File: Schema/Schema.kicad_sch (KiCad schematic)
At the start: 24 parts, among them J1 Battery, SW1 SW_Push, SW2 POWER ON/OFF, SW3 SW_Push, SW4 SW_Push, U1 ATmega328P-P, U2 DS18B20, U3 AM2320, U4 BMP280_Board, U5 E-paper_SSD1681, U6 L7805, U7 LD1117V33, Y1 16M

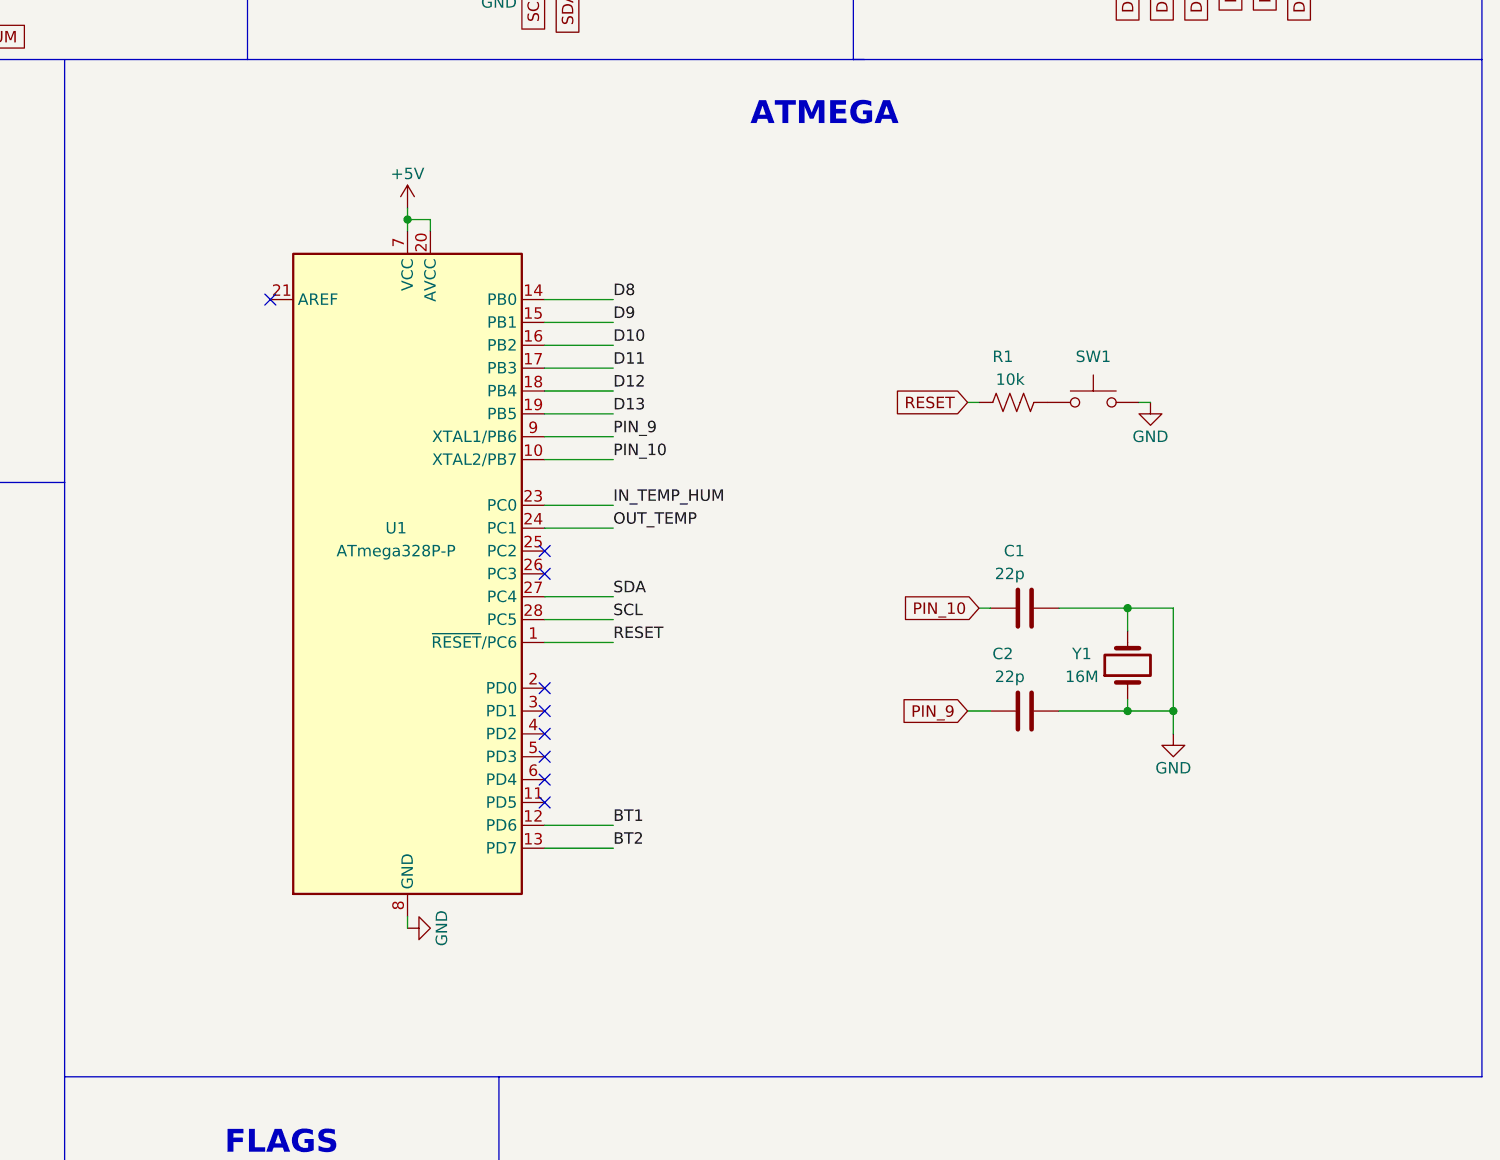
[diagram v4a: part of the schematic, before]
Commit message: Add extra Atmega for tests
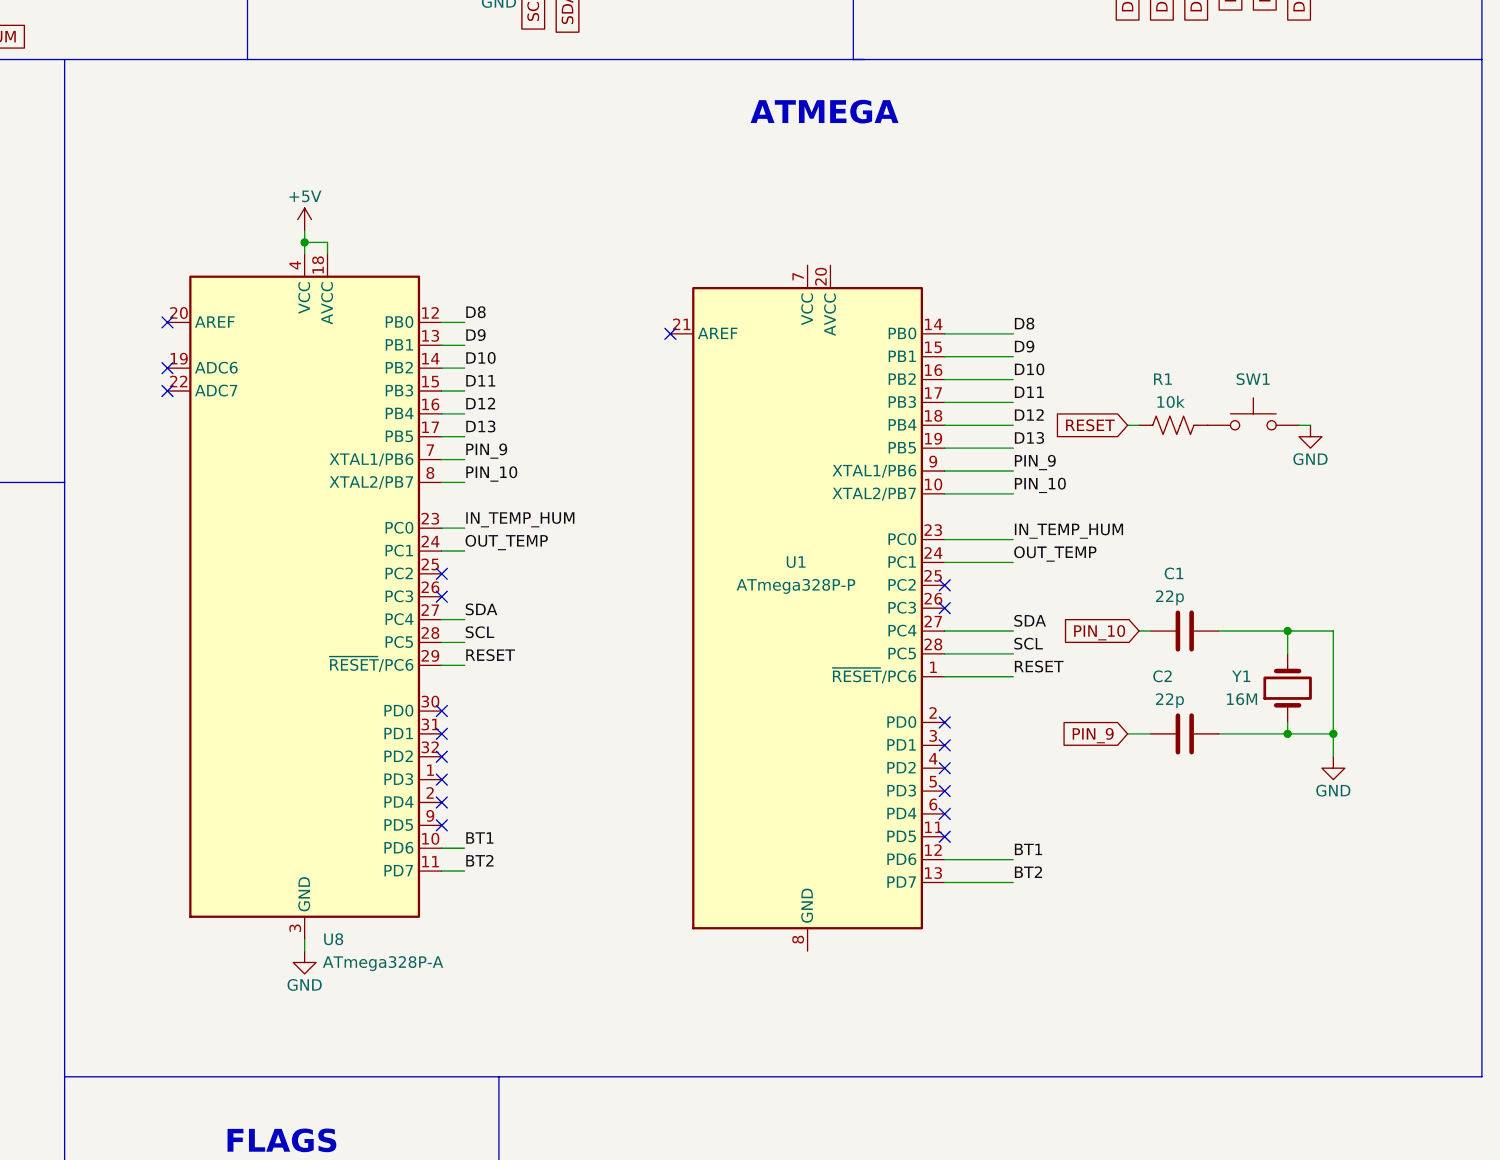
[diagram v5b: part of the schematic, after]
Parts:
- added U8: ATmega328P-A, Package_QFP:TQFP-32_7x7mm_P0.8mm, symbol MCU_Microchip_ATmega:ATmega328P-A
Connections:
- net +5V: now also U8.18 (AVCC), U8.4 (VCC), U8.6 (VCC); no longer U1.20 (AVCC), U1.7 (VCC)
- net BT1: now also U8.10 (PD6)
- net BT2: now also U8.11 (PD7)
- net D10: now also U8.14 (PB2)
- net D11: now also U8.15 (PB3)
- net D12: now also U8.16 (PB4)
- net D13: now also U8.17 (PB5)
- net D8: now also U8.12 (PB0)
- net D9: now also U8.13 (PB1)
- net GND: now also U8.21 (GND), U8.3 (GND), U8.5 (GND); no longer U1.22 (GND), U1.8 (GND)
- net IN_TEMP_HUM: now also U8.23 (PC0)
- net OUT_TEMP: now also U8.24 (PC1)
- net PIN_10: now also U8.8 (XTAL2/PB7)
- net PIN_9: now also U8.7 (XTAL1/PB6)
- net RESET: now also U8.29 (~{RESET}/PC6)
- net SCL: now also U8.28 (PC5)
- net SDA: now also U8.27 (PC4)
- new net: U1.22 (GND), U1.8 (GND)
- no-connect marks 12 -> 23
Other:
- moved on the sheet: C1, C2, R1, SW1, U1, Y1

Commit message: Changed BMP280 --> BMP180 (my sensor turned out to be damaged). Updated some files for clarity.
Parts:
- removed U4: BMP280_Board, symbol SM_Library:BMP280_Board
- added U9: BMP180_Board, symbol SM_Library:BMP180_Board
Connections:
- net +3.3V: now also U9.1
- net +5V: now also U1.20 (AVCC), U1.7 (VCC)
- net GND: now also U1.22 (GND), U1.8 (GND), U9.2
- net SCL: now also U9.3
- net SDA: now also U9.4
- no-connect marks 23 -> 21
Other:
- note added: "BAROMETER AND TEMPRETATURE SENSOR"
- note removed: "BAROMETER SENSOR"

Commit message: #4 Added AM2320 humidity sensor (oneWire). Changed pins for oneWire in Schema.kicad_sch
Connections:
- net IN_TEMP_HUM: now also U1.11 (PD5); no longer U8.23 (PC0)
- net OUT_TEMP: now also U1.4 (PD2); no longer U8.24 (PC1)
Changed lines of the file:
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@@
   (no_connect (at 168.91 107.95))
   (no_connect (at 138.43 80.01))
+  (no_connect (at 168.91 102.87))
   (no_connect (at 36.83 83.82))
+  (no_connect (at 168.91 105.41))
   (no_connect (at 224.79 111.76))
   (no_connect (at 224.79 109.22))
   (no_connect (at 224.79 132.08))
   (no_connect (at 224.79 124.46))
-  (no_connect (at 224.79 129.54))
   (no_connect (at 224.79 134.62))
   (no_connect (at 224.79 127))
-  (no_connect (at 224.79 137.16))
+  (wire (pts (xy 224.79 137.16) (xy 232.41 137.16))
+    (stroke (width 0) (type default) (color 0 0 0 0))
+  )
   (wire (pts (xy 245.11 91.44) (xy 246.38 91.44))
     (stroke (width 0) (type default) (color 0 0 0 0))
@@
     (stroke (width 0) (type default) (color 0 0 0 0))
   )
+  (wire (pts (xy 224.79 129.54) (xy 233.68 129.54))
+    (stroke (width 0) (type default) (color 0 0 0 0))
+  )
   (wire (pts (xy 247.65 114.3) (xy 246.38 114.3))
     (stroke (width 0) (type default) (color 0 0 0 0))
@@
   )
   (wire (pts (xy 156.21 71.12) (xy 156.21 72.39))
-    (stroke (width 0) (type default) (color 0 0 0 0))
-  )
-  (wire (pts (xy 168.91 102.87) (xy 171.45 102.87))
-    (stroke (width 0) (type default) (color 0 0 0 0))
-  )
-  (wire (pts (xy 168.91 105.41) (xy 171.45 105.41))
     (stroke (width 0) (type default) (color 0 0 0 0))
   )
@@
     (effects (font (size 1.27 1.27)) (justify left bottom))
   )
+  (label "IN_TEMP_HUM" (at 232.41 137.16 0)
+    (effects (font (size 1.27 1.27)) (justify left bottom))
+  )
   (label "D10" (at 232.41 86.36 0)
     (effects (font (size 1.27 1.27)) (justify left bottom))
@@
     (effects (font (size 1.27 1.27)) (justify left bottom))
   )
-  (label "OUT_TEMP" (at 171.45 105.41 0)
-    (effects (font (size 1.27 1.27)) (justify left bottom))
-  )
   (label "D8" (at 232.41 81.28 0)
     (effects (font (size 1.27 1.27)) (justify left bottom))
@@
   )
   (label "SCL" (at 232.41 116.84 0)
-    (effects (font (size 1.27 1.27)) (justify left bottom))
-  )
-  (label "IN_TEMP_HUM" (at 171.45 102.87 0)
     (effects (font (size 1.27 1.27)) (justify left bottom))
   )
@@
     (effects (font (size 1.27 1.27)) (justify right bottom))
   )
+  (label "OUT_TEMP" (at 233.68 129.54 0)
+    (effects (font (size 1.27 1.27)) (justify left bottom))
+  )
   (label "BT2" (at 232.41 142.24 0)
